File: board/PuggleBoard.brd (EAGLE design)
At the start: 54.6 x 86.4 mm, 133 parts, among them U1 LMP7704, U10 SN65LVDS2, U11 SN65LVDS1, U12 SN65LVDS1, U13 SN65LVDS1, U14 SN65MLVD201D, U15 24C, U2 ADS8331, U3 OPA4209, U4 AD5686, U5 LTM8045, U6 TPS7A3001, U7 TPS7A4901, U8 REF5040, U9 AD8032

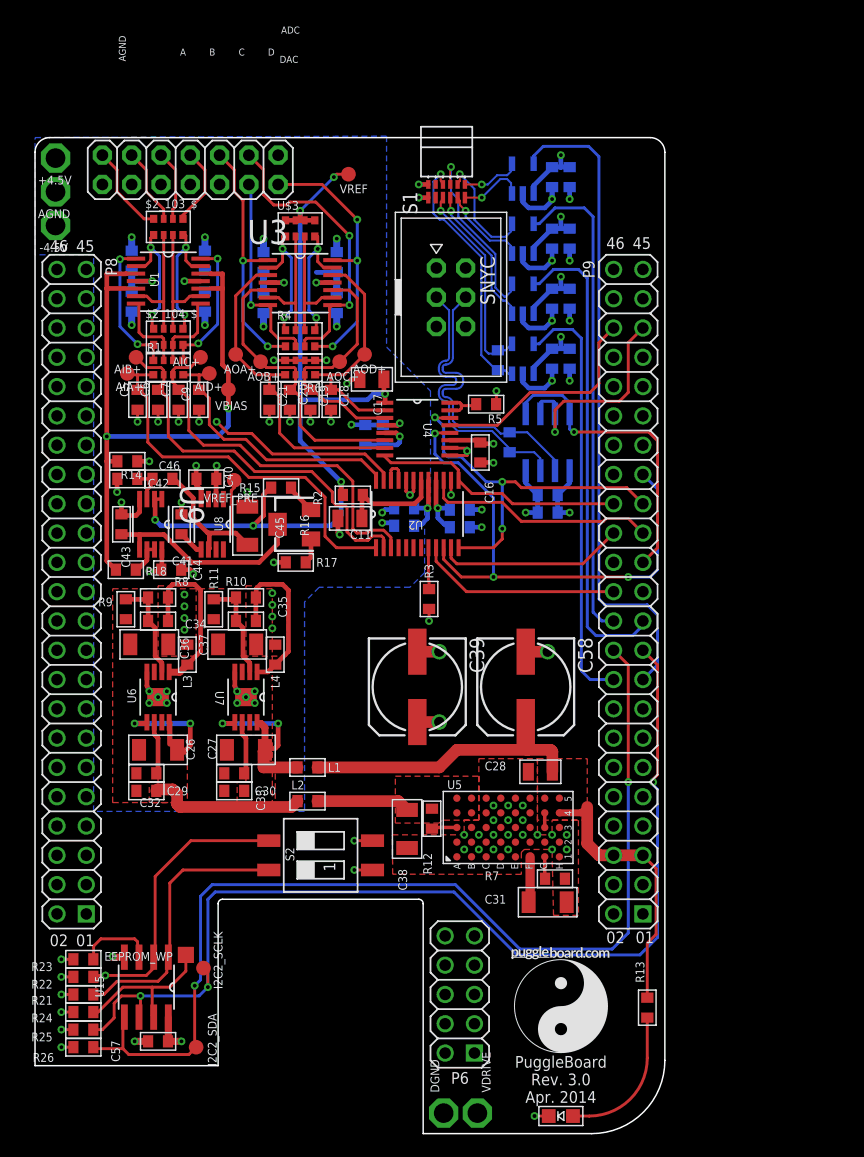
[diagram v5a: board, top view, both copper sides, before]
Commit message: Board is ready for Edgar to look at. There is one strange DRC error, but that can be resolved later. Also, silk screens are a mess, but Edgar can see the layout at least.
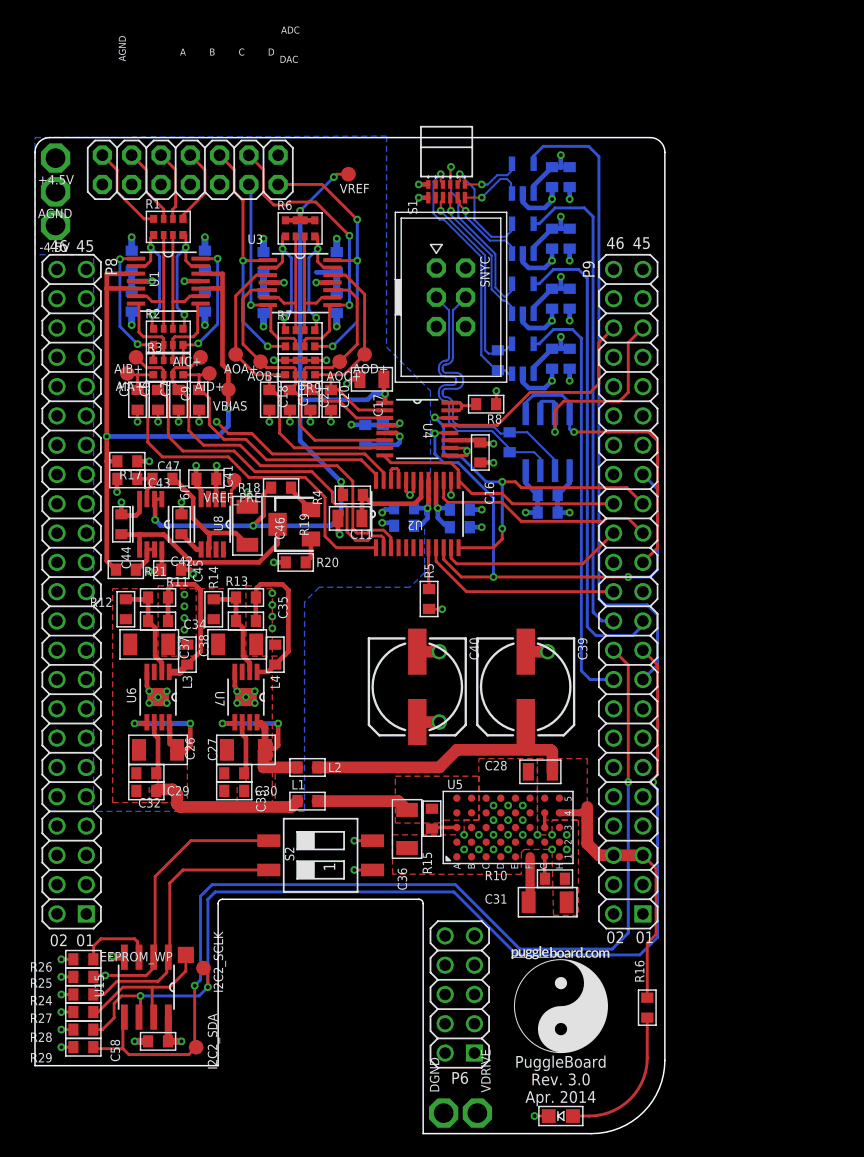
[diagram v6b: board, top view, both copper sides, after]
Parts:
- removed $2_103_$: 2k,ACAS, puggleboard:RX4_0612
- removed $2_104_$: 1k,ACAS, puggleboard:RX4_0612
- removed U$3: (no value), puggleboard:RX4_0612
- added R27: 10k, puggleboard:0603
- added R28, R29: 5.6k, puggleboard:0603
- C36: value 10uF -> 22uF
- C38: value 22uF -> 10uF
- C40: value 1uF -> 47uF; device puggleboard:0603 -> puggleboard:153CLV-0807
- C42: value 0.1uF -> 1uF
- C45: value 4.7uF -> 0.1uF; device puggleboard:1206 -> puggleboard:0603
- C46: value 0.1uF -> 4.7uF; device puggleboard:0603 -> puggleboard:1206
- C51, C56: value 1nF -> 0.1uF
- C55, C57: value 0.1uF -> 1nF
- C58: value 47uF -> 0.1uF; device puggleboard:153CLV-0807 -> puggleboard:0603
- R1: value 1k -> 2k,ACAS; device puggleboard:RX4_0603 -> puggleboard:RX4_0612
- R10: value 13.7k -> 130k
- R11: value 4.7k -> 13.7k
- R12: value 60.4k -> 4.7k
- R13: value 1k -> 13.7k
- R14, R24: value 10k -> 4.7k
- R15: value 6k -> 60.4k
- R16: value 2k -> 1k; device puggleboard:SM-42/43W -> puggleboard:0603
- R17: value 2k -> 10k
- R18: value 10k -> 6k
- R19: value 100 -> 2k; device puggleboard:0603 -> puggleboard:SM-42/43W
- R2: value 10 -> 1k,ACAS; device puggleboard:0603 -> puggleboard:RX4_0612
- R20: value 150 -> 2k
- R21: value 4.7k -> 10k
- R22: value 4.7k -> 100
- R23: value 4.7k -> 150
- R25, R26: value 5.6k -> 4.7k
- R3: value 10k -> 1k; device puggleboard:0603 -> puggleboard:RX4_0603
- R4: value 2k,ACAS -> 10; device puggleboard:RX4_0612 -> puggleboard:0603
- R6: value (none) -> 2k,ACAS; device puggleboard:RX4_0603 -> puggleboard:RX4_0612
- R7: value 130k -> 2k,ACAS; device puggleboard:0603 -> puggleboard:RX4_0612
- R8: value 13.7k -> 10k
- R9: value 4.7k -> (none); device puggleboard:0603 -> puggleboard:RX4_0603
- U14: value SN65MLVD201D -> SN65MLVD201
- moved R22 64.4 mm to (40.1, 67.1), flipped to the bottom, turned to 90 degrees
- moved C57 58.2 mm to (44.5, 55.4), flipped to the bottom
- moved R23 58.1 mm to (41.1, 59.9), flipped to the bottom, turned to 270 degrees
- moved R16 51.9 mm to (53.1, 10.9)
- moved R7 51.8 mm to (23.0, 69.0)
- moved R13 49.8 mm to (18.3, 46.5), turned to 180 degrees
- moved C58 44.3 mm to (10.7, 8.00), turned to 180 degrees
- moved C47 39.4 mm to (8.00, 58.3), flipped to the top, turned to 0 degrees
- moved R21 37.0 mm to (7.87, 48.9), turned to 0 degrees
- moved R10 36.2 mm to (45.1, 22.1), turned to 0 degrees
- moved R8 33.0 mm to (39.1, 63.2), turned to 0 degrees
- moved R12 32.2 mm to (7.87, 45.5)
- moved R15 31.5 mm to (34.4, 27.3), turned to 270 degrees
- moved R3 30.2 mm to (11.6, 66.4), turned to 0 degrees
- moved C55 29.1 mm to (44.8, 82.9), turned to 270 degrees
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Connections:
- net +4.5V: now also C38.1, C41.2, C45.1; no longer C37.1, C40.2, C44.1
- net +4.5V_PRE: now also R13.1; no longer R10.1
- net -4.5V: now also C37.1; no longer C36.1
- net -4.5V_PRE: now also R11.1; no longer R8.1
- net ADC_-IN_A: now also R1.P1, R2.P2; no longer $2_103_$.P1, $2_104_$.P2
- net ADC_-IN_B: now also R1.P3, R2.P4; no longer $2_103_$.P3, $2_104_$.P4
- net ADC_-IN_C: now also R1.P5, R2.P6; no longer $2_103_$.P5, $2_104_$.P6
- net ADC_-IN_D: now also R1.P7, R2.P8; no longer $2_103_$.P7, $2_104_$.P8
- net ADC_A: now also R1.P2; no longer $2_103_$.P2
- net ADC_A+: now also R2.P1, R3.P2; no longer $2_104_$.P1, R1.P2
- net ADC_B: now also R1.P4; no longer $2_103_$.P4
- net ADC_B+: now also R2.P3, R3.P4; no longer $2_104_$.P3, R1.P4
- net ADC_C: now also R1.P6; no longer $2_103_$.P6
- net ADC_C+: now also R2.P5, R3.P6; no longer $2_104_$.P5, R1.P6
- net ADC_D: now also R1.P8; no longer $2_103_$.P8
- net ADC_D+: now also R2.P7, R3.P8; no longer $2_104_$.P7, R1.P8
- net AGND1: now also R13.2, R14.1; no longer R10.2, R11.1
- net AGND2: now also R11.2, R12.1; no longer R8.2, R9.1
- net DAC_+IN_A: now also C18.1, R9.P8; no longer C21.1, R6.P8
- net DAC_+IN_B: now also C19.1, R9.P6; no longer C20.1, R6.P6
- net DAC_+IN_C: now also C21.1, R9.P4; no longer C19.1, R6.P4
- net DAC_+IN_D: now also C20.1, R9.P2; no longer C18.1, R6.P2
- net DAC_-IN_A: now also R6.P1, R7.P2; no longer R4.P2, U$3.P1
- net DAC_-IN_B: now also R6.P3, R7.P4; no longer R4.P4, U$3.P3
- net DAC_-IN_C: now also R6.P5, R7.P6; no longer R4.P6, U$3.P5
- net DAC_-IN_D: now also R6.P7, R7.P8; no longer R4.P8, U$3.P7
- net DAC_A: now also R7.P1; no longer R4.P1
- net DAC_B: now also R7.P3; no longer R4.P3
- net DAC_C: now also R7.P5; no longer R4.P5
- net DAC_D: now also R7.P7; no longer R4.P7
- net GND: now also C40.-, C42.1, C58.2, R10.2, R12.2, R14.2, R20.2, R9.P1, R9.P3, R9.P5, R9.P7; no longer C40.1, C42.2, C58.-, R11.2, R17.2, R6.P1, R6.P3, R6.P5, R6.P7, R7.2, R9.2
- net I2C2_SCL: now also R28.1; no longer R25.1
- net I2C2_SDA: now also R29.1; no longer R26.1
- net MISO1_N: now also R22.2; no longer R19.2
- net MISO1_P: now also R22.1; no longer R19.1
- net N$10: now also R18.2, R19.3; no longer R15.2, R16.3
- net N$14: now also R24.1; no longer R21.1
- net N$16: now also R4.1; no longer R2.1
- net N$18: now also R25.1; no longer R22.1
- net N$19: now also R26.1; no longer R23.1
- net N$20: now also R16.1; no longer R13.1
- net N$22: now also R27.1; no longer R24.1
- net N$28: now also C43.1, R17.1; no longer C42.1, R14.1
- net N$32: now also C42.2; no longer C41.2
- net N$37: now also R10.1; no longer R7.1
- net N$4: now also C44.1, R19.2; no longer C43.1, R16.2
- net N$40: now also R3.P1; no longer R1.P1
- net N$41: now also R3.P3; no longer R1.P3
- net N$42: now also R3.P5; no longer R1.P5
- net N$43: now also R3.P7; no longer R1.P7
- net N$45: now also R15.2; no longer R12.2
- net N$8: now also R19.1, R20.1; no longer R16.1, R17.1
- net N$9: now also R21.2; no longer R18.2
- net SYNC_N: now also R23.2; no longer R20.2
- net SYNC_P: now also R23.1; no longer R20.1
- net VBIAS: now also C47.1, R21.1; no longer C46.1, R18.1
- net VDD_5V: now also C39.+, L2.1, R16.2; no longer C58.+, L1.1, R13.2
- net VDD_POST_LC: now also L2.2; no longer L1.2
- net VDRIVE: now also C40.+, C58.1, R27.2, R28.2, R29.2, R8.2; no longer C39.+, C47.1, R21.2, R22.2, R23.2, R3.2
- net VOUT-: now also C36.1, L1.1, R15.1; no longer C38.1, L2.1, R12.1
- net VREF: now also R18.1, R4.2, R6.P2, R6.P4, R6.P6, R6.P8; no longer R15.1, R2.2, U$3.P2, U$3.P4, U$3.P6, U$3.P8
- net VREF_PRE: now also C46.1, R17.2; no longer C45.1, R14.2
- net VSS_POST_LC: now also L1.2; no longer L2.2
- net ~ADCRST: now also R5.1; no longer R3.1
- net ~DACRST: now also R8.1; no longer R5.1

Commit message: Minor changes.
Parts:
- moved U$2 108.4 mm to (21.1, 22.4), turned to 90 degrees
- moved A_I/O 2.34 mm to (15.7, 83.1)
- renumbered I2C2_SCLK to SCLK, I2C2_SDA to SDA, VDRIVE to 3.3V
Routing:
- net VREF: track 71.4 -> 76.5 mm
- net DAC_C: track 25.9 -> 23.1 mm
- net DAC_D: track 23.7 -> 21.3 mm
- net ADC_D: track 6.84 -> 6.22 mm
- net ADC_C: track 6.16 -> 5.55 mm
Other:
- board text removed: "A"
- board text removed: "ADC"
- board text removed: "AGND"
- board text removed: "B"
- board text removed: "C"
- board text removed: "D"
- board text removed: "DAC"

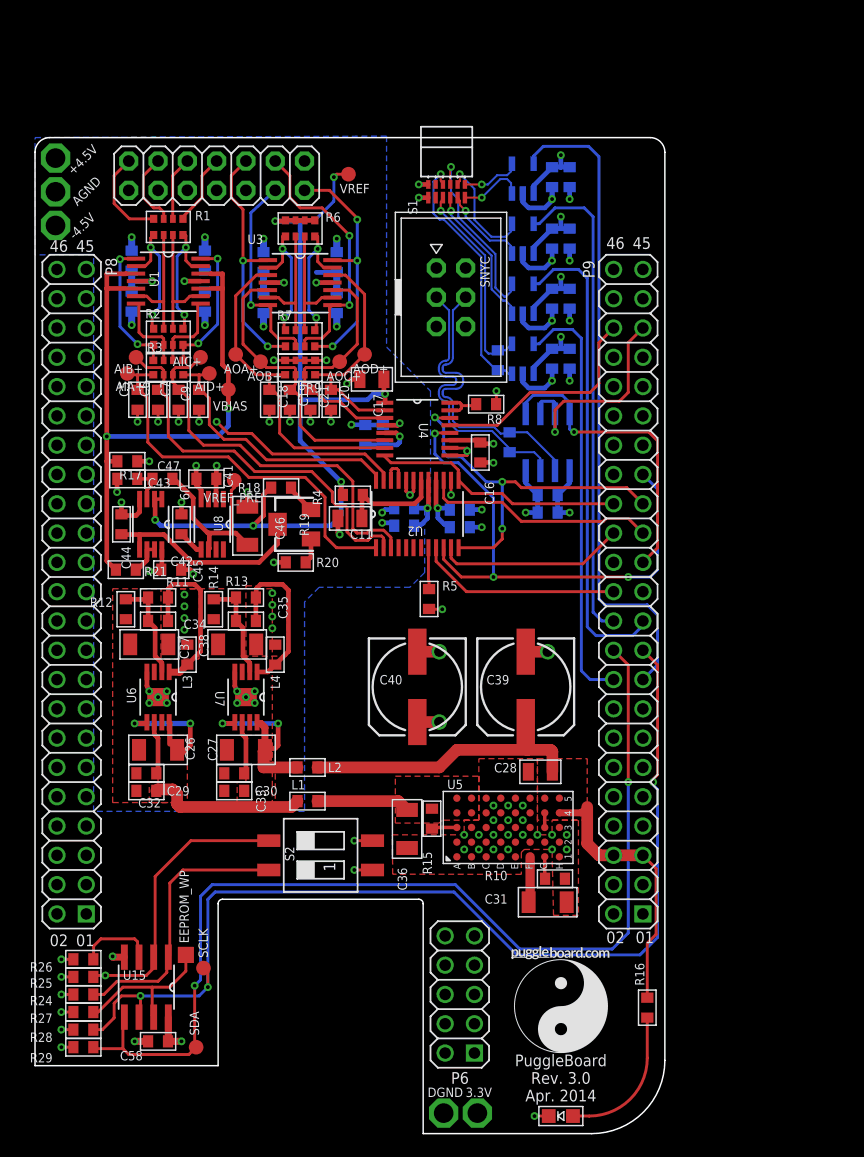
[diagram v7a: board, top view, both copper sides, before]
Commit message: Impletemented Edgar's suggestions from our meeting. Should be nearing the silkscreen finalization stage.
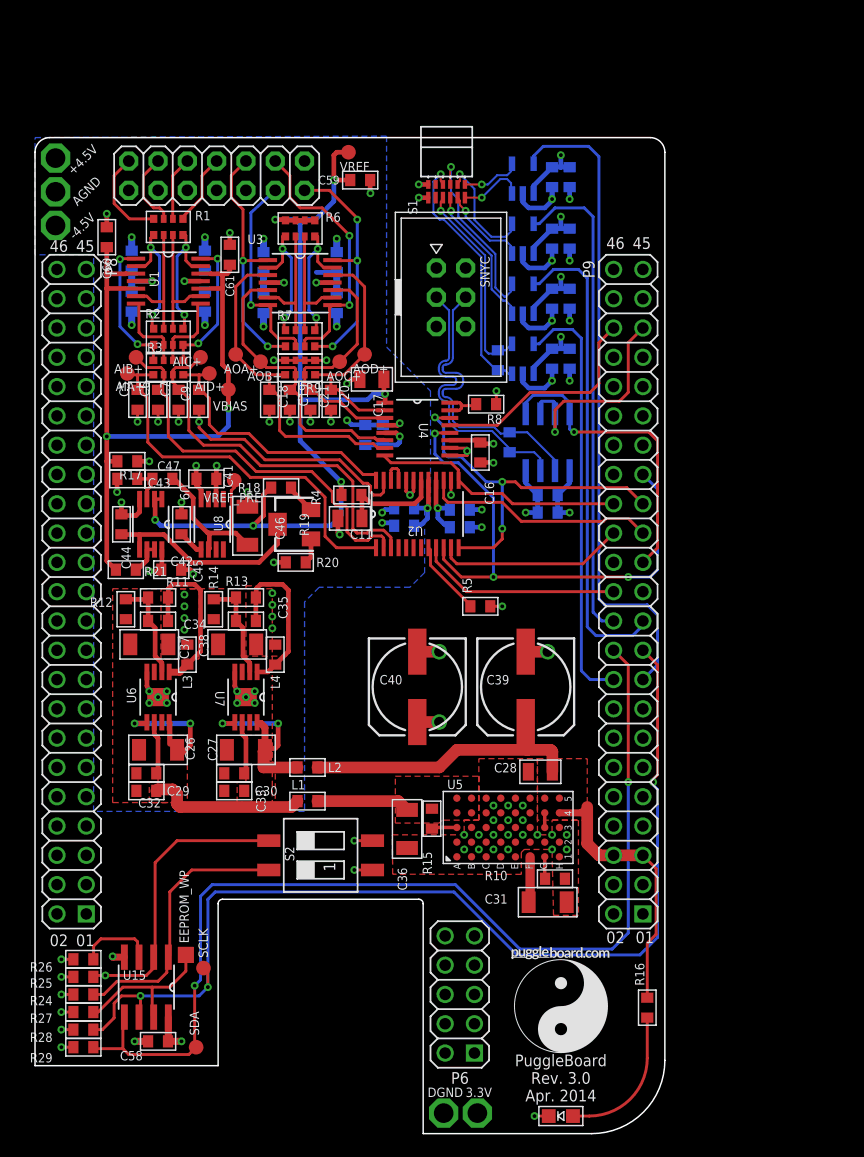
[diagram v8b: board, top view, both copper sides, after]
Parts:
- added C59, C60, C61: 0.1uF, puggleboard:0603
- moved R5 4.49 mm to (38.6, 45.7), turned to 0 degrees
- moved VREF 1.91 mm to (27.2, 85.1)
- moved R4 0.13 mm to (27.4, 55.4)
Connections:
- net GND: now also C59.2, C60.2, C61.2
- net VBIAS: now also C60.1, C61.1
- net VREF: now also C59.1
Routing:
- net GND: track 122.6 -> 128.2 mm, vias 86 -> 88
- net VBIAS: track 60.1 -> 63.7 mm
- net ~ADCRST: track 3.60 -> 6.58 mm
- net VREF: track 76.5 -> 77.7 mm
- net N$18: track 24.9 -> 25.6 mm
